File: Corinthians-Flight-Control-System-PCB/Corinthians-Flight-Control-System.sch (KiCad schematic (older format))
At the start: 81 parts, among them J0 RaspberryPi, J1 50ohm Coaxial Ant, J10 M8, J11 M9, J12 M10, J2 GPS/Compass, J3 M1, J4 M2, J5 M3, J6 M4, J7 M5, J8 M6, J9 M7, SW1 BootSW, SW2 SW_DIP_x01, SW3 SW_s, U1 STM32F103C8Tx, U2 LSM6DS3, U3 BMP280, U4 NRF24L01, U5 IST8310, U6 AMS1117-3.3, U7 AMS1117-5.0, Y1 8Mhz, Y2 16Mhz

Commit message: New corrections and CAD files
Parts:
- F1: value 500mA -> 3A
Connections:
- net CE: now also U1.26 (PB13); no longer U1.14 (PA4)
- net CSN: now also U1.27 (PB14); no longer U1.15 (PA5)
- net MISO: now also U1.16 (PA6); no longer U1.40 (PB4)
- net MOSI: now also U1.17 (PA7); no longer U1.41 (PB5)
- net PWM1-E: now also U1.40 (PB4); no longer U1.26 (PB13)
- net PWM1-F: now also U1.41 (PB5); no longer U1.27 (PB14)
- net PWM1-G: now also U1.18 (PB0); no longer U1.28 (PB15)
- net SCK: now also U1.15 (PA5); no longer U1.39 (PB3)
- net SW_s: now also U1.28 (PB15)
- no-connect marks 53 -> 52
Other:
- moved on the sheet: R4, R5
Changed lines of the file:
@@
 Wire Wire Line
 	10100 3200 10100 3150
-Text GLabel 9100 5400 0    50   Input ~ 0
+Text GLabel 8600 5400 0    50   Input ~ 0
 SDA
-Text GLabel 9100 5300 0    50   Input ~ 0
-SCL
 Text GLabel 10600 5400 2    50   Input ~ 0
 PWM1-B
@@
 Text GLabel 10600 5600 2    50   Input ~ 0
 PWM1-D
-Text GLabel 9100 6000 0    50   Input ~ 0
+Text GLabel 9150 4500 0    50   Input ~ 0
 PWM1-G
-Text GLabel 9100 5900 0    50   Input ~ 0
+Text GLabel 9150 5000 0    50   Input ~ 0
 PWM1-F
-Text GLabel 9100 5800 0    50   Input ~ 0
+Text GLabel 9150 4900 0    50   Input ~ 0
 PWM1-E
 Wire Wire Line
@@
 Wire Wire Line
 	8350 4200 8350 4150
-Text GLabel 9100 5000 0    50   Input ~ 0
+Text GLabel 10600 5200 2    50   Input ~ 0
 MOSI
-Text GLabel 9100 4900 0    50   Input ~ 0
-MISO
-Text GLabel 9100 4800 0    50   Input ~ 0
+Text GLabel 10600 5000 2    50   Input ~ 0
 SCK
 $Comp
@@
 	8350 3750 8350 4150
 Wire Wire Line
-	9100 6000 9200 6000
-Wire Wire Line
-	9100 5900 9200 5900
-Wire Wire Line
-	9100 5800 9200 5800
-Wire Wire Line
 	9100 5700 9200 5700
 Wire Wire Line
@@
 	9100 5500 9200 5500
 Wire Wire Line
-	9100 5400 9150 5400
-Wire Wire Line
 	9100 5200 9200 5200
 Wire Wire Line
 	9100 5100 9200 5100
 Wire Wire Line
-	9100 5000 9200 5000
-Wire Wire Line
-	9100 4900 9200 4900
-Wire Wire Line
-	9100 4800 9200 4800
+	10600 5200 10500 5200
 Wire Wire Line
 	10550 5800 10500 5800
@@
 NoConn ~ 1500 6100
 NoConn ~ 10500 5700
-NoConn ~ 10500 5200
-NoConn ~ 10500 5100
-NoConn ~ 9200 4500
-NoConn ~ 9200 4600
-NoConn ~ 9200 4700
 Wire Wire Line
 	6250 1150 6400 1150
@@
 L Device:R_Small R5
 U 1 1 5FAD2178
-P 8850 5200
-F 0 "R5" V 8654 5200 50  0000 C CNN
-F 1 "4.7K" V 8745 5200 50  0000 C CNN
-F 2 "Resistor_SMD:R_0402_1005Metric" H 8850 5200 50  0001 C CNN
-F 3 "~" H 8850 5200 50  0001 C CNN
-	1    8850 5200
+P 8650 5150
+F 0 "R5" V 8454 5150 50  0000 C CNN
+F 1 "4.7K" V 8545 5150 50  0000 C CNN
+F 2 "Resistor_SMD:R_0402_1005Metric" H 8650 5150 50  0001 C CNN
+F 3 "~" H 8650 5150 50  0001 C CNN
+	1    8650 5150
 	1    0    0    -1
 $EndComp
@@
 L power:+3.3V #PWR0131
 U 1 1 5FB2B0E2
-P 8850 4700
-F 0 "#PWR0131" H 8850 4550 50  0001 C CNN
-F 1 "+3.3V" H 8865 4873 50  0000 C CNN
-F 2 "" H 8850 4700 50  0001 C CNN
-F 3 "" H 8850 4700 50  0001 C CNN
-	1    8850 4700
+P 8650 4700
+F 0 "#PWR0131" H 8650 4550 50  0001 C CNN
+F 1 "+3.3V" H 8665 4873 50  0000 C CNN
+F 2 "" H 8650 4700 50  0001 C CNN
+F 3 "" H 8650 4700 50  0001 C CNN
+	1    8650 4700
 	1    0    0    -1
 $EndComp
@@
 L power:+3.3V #PWR0152
 U 1 1 5FB3CB59
-P 8600 5050
-F 0 "#PWR0152" H 8600 4900 50  0001 C CNN
-F 1 "+3.3V" H 8615 5223 50  0000 C CNN
-F 2 "" H 8600 5050 50  0001 C CNN
-F 3 "" H 8600 5050 50  0001 C CNN
-	1    8600 5050
-	1    0    0    -1
-$EndComp
-Wire Wire Line
-	8850 5100 8850 4700
-Wire Wire Line
-	9100 5300 9150 5300
-Wire Wire Line
-	8900 5350 9150 5350
-Wire Wire Line
-	9150 5350 9150 5400
-Connection ~ 9150 5400
-Wire Wire Line
-	9150 5400 9200 5400
-Wire Wire Line
-	8850 5300 8900 5300
-Wire Wire Line
-	8900 5300 8900 5250
-Wire Wire Line
-	8900 5250 9150 5250
-Wire Wire Line
-	9150 5250 9150 5300
-Connection ~ 9150 5300
-Wire Wire Line
-	9150 5300 9200 5300
-Wire Wire Line
-	8600 5350 8600 5050
+P 8350 4700
+F 0 "#PWR0152" H 8350 4550 50  0001 C CNN
+F 1 "+3.3V" H 8365 4873 50  0000 C CNN
+F 2 "" H 8350 4700 50  0001 C CNN
+F 3 "" H 8350 4700 50  0001 C CNN
+	1    8350 4700
+	1    0    0    -1
+$EndComp
 $Comp
 L Device:R_Small R4
 U 1 1 5FABF7FE
-P 8600 5450
-F 0 "R4" V 8404 5450 50  0000 C CNN
-F 1 "4.7K" V 8495 5450 50  0000 C CNN
-F 2 "Resistor_SMD:R_0402_1005Metric" H 8600 5450 50  0001 C CNN
-F 3 "~" H 8600 5450 50  0001 C CNN
-	1    8600 5450
+P 8350 5150
+F 0 "R4" V 8154 5150 50  0000 C CNN
+F 1 "4.7K" V 8245 5150 50  0000 C CNN
+F 2 "Resistor_SMD:R_0402_1005Metric" H 8350 5150 50  0001 C CNN
+F 3 "~" H 8350 5150 50  0001 C CNN
+	1    8350 5150
 	1    0    0    -1
 $EndComp
@@
 	8550 4350 8550 4150
 Connection ~ 8550 4150
-Text GLabel 10600 4900 2    50   Input ~ 0
+Text GLabel 9100 5800 0    50   Input ~ 0
 CE
-Wire Wire Line
-	10600 4900 10500 4900
 $Comp
 L Switch:SW_DIP_x01 SW2
@@
 Wire Wire Line
 	8150 700  8150 850
-Text GLabel 10600 5000 2    50   Input ~ 0
+Text GLabel 9100 5900 0    50   Input ~ 0
 CSN
-Wire Wire Line
-	10000 6200 9900 6200
-Connection ~ 9900 6200
-Wire Wire Line
-	9900 6200 9800 6200
-Connection ~ 9800 6200
-Wire Wire Line
-	9700 6200 9800 6200
-Wire Wire Line
-	9700 6200 9600 6200
-Connection ~ 9700 6200
-Wire Wire Line
-	10000 3200 9900 3200
-Connection ~ 9900 3200
-Wire Wire Line
-	9800 3200 9900 3200
-Wire Wire Line
-	9700 3200 9800 3200
-Connection ~ 9800 3200
-Connection ~ 9700 3200
-$Comp
-L MCU_ST_STM32F1:STM32F103C8Tx U1
-U 1 1 5F8FC5F0
-P 9900 4700
-F 0 "U1" H 9850 3111 50  0000 C CNN
-F 1 "STM32F103C8Tx" H 9850 3020 39  0000 C CNN
-F 2 "Package_QFP:LQFP-48_7x7mm_P0.5mm" H 9300 3300 50  0001 R CNN
-F 3 "http://www.st.com/st-web-ui/static/active/en/resource/technical/document/datasheet/CD00161566.pdf" H 9900 4700 50  0001 C CNN
-	1    9900 4700
-	1    0    0    -1
-$EndComp
 Wire Wire Line
 	10600 5000 10500 5000
@@
 P 3000 1000
 F 0 "F1" H 3000 1169 50  0000 C CNN
-F 1 "500mA" H 3000 1086 39  0000 C CNN
+F 1 "3A" H 3000 1086 39  0000 C CNN
 F 2 "Fuse:Fuse_0805_2012Metric" H 3000 1000 50  0001 C CNN
 F 3 "~" H 3000 1000 50  0001 C CNN
@@
 Wire Wire Line
 	2650 800  2650 1000
-Wire Wire Line
-	8600 5550 8900 5550
-Wire Wire Line
-	8900 5550 8900 5350
 Text GLabel 9100 5500 0    50   Input ~ 0
 TX2
@@
 	1    0    0    -1
 $EndComp
+Text GLabel 10600 5100 2    50   Input ~ 0
+MISO
+Connection ~ 9700 3200
+Connection ~ 9800 3200
+Wire Wire Line
+	9700 3200 9800 3200
+Connection ~ 9900 3200
+Wire Wire Line
+	9800 3200 9900 3200
+Wire Wire Line
+	10000 3200 9900 3200
+Connection ~ 9700 6200
+Wire Wire Line
+	9700 6200 9600 6200
+Wire Wire Line
+	9700 6200 9800 6200
+Connection ~ 9800 6200
+Connection ~ 9900 6200
+Wire Wire Line
+	9900 6200 9800 6200
+Wire Wire Line
+	10000 6200 9900 6200
+$Comp
+L MCU_ST_STM32F1:STM32F103C8Tx U1
+U 1 1 5F8FC5F0
+P 9900 4700
+F 0 "U1" H 9850 3111 50  0000 C CNN
+F 1 "STM32F103C8Tx" H 9850 3020 39  0000 C CNN
+F 2 "Package_QFP:LQFP-48_7x7mm_P0.5mm" H 9300 3300 50  0001 R CNN
+F 3 "http://www.st.com/st-web-ui/static/active/en/resource/technical/document/datasheet/CD00161566.pdf" H 9900 4700 50  0001 C CNN
+	1    9900 4700
+	1    0    0    -1
+$EndComp
+Wire Wire Line
+	10500 5100 10600 5100
+Wire Wire Line
+	8650 5050 8650 4700
+Wire Wire Line
+	8650 5250 8650 5300
+Connection ~ 8650 5300
+Wire Wire Line
+	8650 5300 8600 5300
+Text GLabel 8600 5300 0    50   Input ~ 0
+SCL
+Wire Wire Line
+	8650 5400 8650 5350
+Wire Wire Line
+	8650 5350 8350 5350
+Wire Wire Line
+	8350 5350 8350 5250
+Connection ~ 8650 5400
+Wire Wire Line
+	8650 5400 8600 5400
+Wire Wire Line
+	8350 5050 8350 4700
+Wire Wire Line
+	9150 4900 9200 4900
+Wire Wire Line
+	9150 5000 9200 5000
+Wire Wire Line
+	9150 4500 9200 4500
+Wire Wire Line
+	8650 5300 9200 5300
+Wire Wire Line
+	8650 5400 9200 5400
+Text GLabel 9100 6000 0    50   Input ~ 0
+SW_s
+NoConn ~ 9200 4700
+NoConn ~ 9200 4800
+Wire Wire Line
+	9100 5800 9200 5800
+Wire Wire Line
+	9100 5900 9200 5900
+NoConn ~ 10500 4900
+Wire Wire Line
+	9100 6000 9200 6000
+NoConn ~ 9200 4600
 $EndSCHEMATC

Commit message: updates
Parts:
- removed R15: 10K, Resistor_SMD:R_0402_1005Metric, symbol Device:R_Small
- added C30: 0.1uF, Capacitor_SMD:C_0402_1005Metric, symbol Device:C_Small
- C10, C11, C19, C20: footprint Capacitor_SMD:C_0603_1608Metric -> Capacitor_SMD:C_0805_2012Metric
- renumbered R14 to R10, R16 to R11, R17 to R12
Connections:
- net GND: now also SW2.1, C30.1, C30.2
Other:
- note added: "3.3v linear voltage regulator\npowers all ICs and smd components\nInput from ESC 5v BEC 0805 caps"
- note added: "5v regulator for external\nGPS and Compass. Input\nfrom ESC 5v BEC, 0805 C, 0805 F1, D6, FB1"
- note removed: "3.3v linear voltage regulator\npowers all ICs and smd components\nInput from ESC 5v BEC 0603 caps"
- note removed: "5v regulator for external\nGPS and Compass. Input\nfrom ESC 5v BEC, 0603 C, 0805 F1, D6, FB1"
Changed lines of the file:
@@
 	5900 550  5900 1850
-Wire Notes Line
-	5900 1850 4450 1850
 Wire Notes Line
 	4450 1850 4450 550
@@
 Wire Notes Line
 	5250 2200 5250 4200
-Wire Notes Line
-	3050 2200 5250 2200
 NoConn ~ 3450 3550
 NoConn ~ 3450 2950
@@
 F 0 "C11" H 2192 1338 50  0000 L CNN
 F 1 "10uF" H 2192 1255 39  0000 L CNN
-F 2 "Capacitor_SMD:C_0603_1608Metric" H 2100 1300 50  0001 C CNN
+F 2 "Capacitor_SMD:C_0805_2012Metric" H 2100 1300 50  0001 C CNN
 F 3 "~" H 2100 1300 50  0001 C CNN
 	1    2100 1300
@@
 F 0 "C10" H 1542 1338 50  0000 L CNN
 F 1 "10uF" H 1542 1255 39  0000 L CNN
-F 2 "Capacitor_SMD:C_0603_1608Metric" H 1450 1300 50  0001 C CNN
+F 2 "Capacitor_SMD:C_0805_2012Metric" H 1450 1300 50  0001 C CNN
 F 3 "~" H 1450 1300 50  0001 C CNN
 	1    1450 1300
@@
 Connection ~ 8350 4150
 $Comp
-L Device:R_Small R14
+L Device:R_Small R10
 U 1 1 5FC8FB39
 P 8650 4350
-F 0 "R14" V 8454 4350 50  0000 C CNN
+F 0 "R10" V 8454 4350 50  0000 C CNN
 F 1 "...." V 8545 4350 50  0000 C CNN
 F 2 "Resistor_SMD:R_0402_1005Metric" H 8650 4350 50  0001 C CNN
@@
 	1    0    0    -1
 $EndComp
-$Comp
-L Device:R_Small R15
-U 1 1 601F7C14
-P 4600 900
-F 0 "R15" V 4796 900 50  0000 C CNN
-F 1 "10K" V 4705 900 39  0000 C CNN
-F 2 "Resistor_SMD:R_0402_1005Metric" H 4600 900 50  0001 C CNN
-F 3 "~" H 4600 900 50  0001 C CNN
-	1    4600 900
-	1    0    0    -1
-$EndComp
 Text GLabel 5550 1300 2    50   Input ~ 0
 NRST
@@
 L power:GND #PWR0153
 U 1 1 6025A3C2
-P 4650 700
-F 0 "#PWR0153" H 4650 450 50  0001 C CNN
-F 1 "GND" H 4655 527 50  0000 C CNN
-F 2 "" H 4650 700 50  0001 C CNN
-F 3 "" H 4650 700 50  0001 C CNN
-	1    4650 700
-	0    -1   -1   0
+P 4600 800
+F 0 "#PWR0153" H 4600 550 50  0001 C CNN
+F 1 "GND" H 4605 627 50  0000 C CNN
+F 2 "" H 4600 800 50  0001 C CNN
+F 3 "" H 4600 800 50  0001 C CNN
+	1    4600 800
+	-1   0    0    1
 $EndComp
 Wire Wire Line
@@
 $EndComp
 $Comp
-L Device:R_Small R16
+L Device:R_Small R11
 U 1 1 60310E55
 P 8150 950
-F 0 "R16" V 7954 950 50  0000 C CNN
+F 0 "R11" V 7954 950 50  0000 C CNN
 F 1 "470" V 8045 950 50  0000 C CNN
 F 2 "Resistor_SMD:R_0402_1005Metric" H 8150 950 50  0001 C CNN
@@
 	5550 1300 5450 1300
 Wire Wire Line
-	4650 700  4600 700
-Wire Wire Line
-	4600 700  4600 800
-Wire Wire Line
 	4950 950  4950 900
 Wire Wire Line
-	4850 1000 4600 1000
-Wire Wire Line
-	4850 1300 4850 1000
+	4850 1050 4600 1050
+Wire Wire Line
+	4850 1300 4850 1050
 Wire Wire Line
 	5700 950  5700 1050
@@
 L power:GND #PWR0177
 U 1 1 605B4224
-P 4650 1250
-F 0 "#PWR0177" H 4650 1000 50  0001 C CNN
-F 1 "GND" H 4655 1077 50  0000 C CNN
-F 2 "" H 4650 1250 50  0001 C CNN
-F 3 "" H 4650 1250 50  0001 C CNN
-	1    4650 1250
+P 4650 1300
+F 0 "#PWR0177" H 4650 1050 50  0001 C CNN
+F 1 "GND" H 4655 1127 50  0000 C CNN
+F 2 "" H 4650 1300 50  0001 C CNN
+F 3 "" H 4650 1300 50  0001 C CNN
+	1    4650 1300
 	-1   0    0    1
 $EndComp
@@
 $EndComp
 $Comp
-L Device:R_Small R17
+L Device:R_Small R12
 U 1 1 605B4230
 P 5200 1450
-F 0 "R17" V 5396 1450 50  0000 C CNN
+F 0 "R12" V 5396 1450 50  0000 C CNN
 F 1 "10K" V 5305 1450 39  0000 C CNN
 F 2 "Resistor_SMD:R_0402_1005Metric" H 5200 1450 50  0001 C CNN
@@
 	4650 1550 4650 1600
 Wire Wire Line
-	4650 1350 4650 1250
+	4650 1350 4650 1300
 Wire Wire Line
 	5400 1450 5400 1650
@@
 All passive smd components are \n0402  unless otherwise stated
 Text Notes 600  1850 0    50   ~ 0
-3.3v linear voltage regulator\npowers all ICs and smd components\nInput from ESC 5v BEC 0603 caps
+3.3v linear voltage regulator\npowers all ICs and smd components\nInput from ESC 5v BEC 0805 caps
 Text Notes 600  4200 0    50   ~ 0
 Internal compass IC
@@
 $EndComp
 Text Notes 2550 1850 0    50   ~ 0
-5v regulator for external\nGPS and Compass. Input\nfrom ESC 5v BEC, 0603 C, 0805 F1, D6, FB1
+5v regulator for external\nGPS and Compass. Input\nfrom ESC 5v BEC, 0805 C, 0805 F1, D6, FB1
 $Comp
 L power:+5VD #PWR0138
@@
 F 0 "C20" H 4092 1338 50  0000 L CNN
 F 1 "10uF" H 4092 1255 39  0000 L CNN
-F 2 "Capacitor_SMD:C_0603_1608Metric" H 4000 1300 50  0001 C CNN
+F 2 "Capacitor_SMD:C_0805_2012Metric" H 4000 1300 50  0001 C CNN
 F 3 "~" H 4000 1300 50  0001 C CNN
 	1    4000 1300
@@
 F 0 "C19" H 3442 1338 50  0000 L CNN
 F 1 "10uF" H 3442 1255 39  0000 L CNN
-F 2 "Capacitor_SMD:C_0603_1608Metric" H 3350 1300 50  0001 C CNN
+F 2 "Capacitor_SMD:C_0805_2012Metric" H 3350 1300 50  0001 C CNN
 F 3 "~" H 3350 1300 50  0001 C CNN
 	1    3350 1300
@@
 	9100 6000 9200 6000
 NoConn ~ 9200 4600
+$Comp
+L Device:C_Small C30
+U 1 1 610C7966
+P 4750 950
+F 0 "C30" H 4842 988 50  0000 L CNN
+F 1 "0.1uF" H 4842 905 39  0000 L CNN
+F 2 "Capacitor_SMD:C_0402_1005Metric" H 4750 950 50  0001 C CNN
+F 3 "~" H 4750 950 50  0001 C CNN
+	1    4750 950
+	0    -1   -1   0
+$EndComp
+Wire Notes Line
+	3050 2200 5250 2200
+Wire Notes Line
+	5900 1850 4450 1850
+Wire Wire Line
+	4600 1050 4600 950
+Wire Wire Line
+	4600 950  4650 950
+Connection ~ 4600 950
+Wire Wire Line
+	4600 850  4850 850
+Wire Wire Line
+	4850 850  4850 950
+Connection ~ 4600 850
+Wire Wire Line
+	4600 850  4600 950
+Wire Wire Line
+	4600 800  4600 850
 $EndSCHEMATC

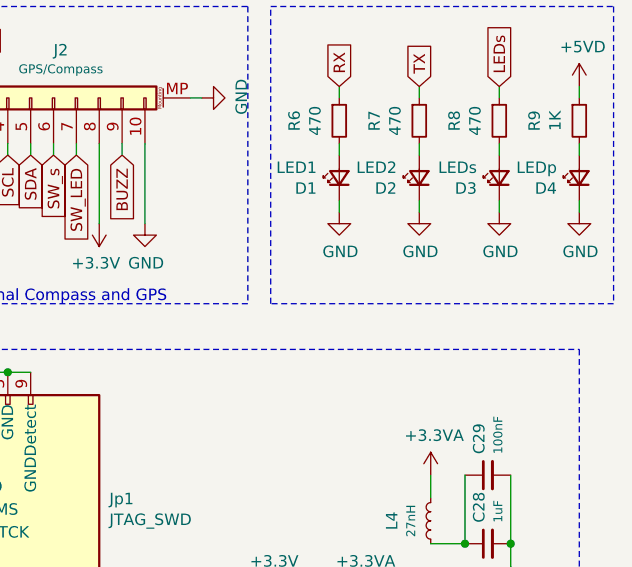
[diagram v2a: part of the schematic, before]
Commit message: schematic and pcb routing update
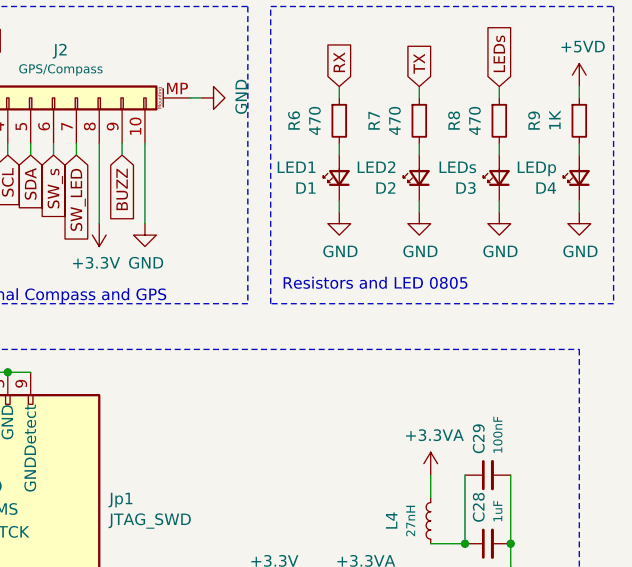
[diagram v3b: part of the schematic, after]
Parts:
- D1, D2, D3, D4: footprint LED_SMD:LED_0402_1005Metric -> LED_SMD:LED_0805_2012Metric
- R6, R7, R8, R9: footprint Resistor_SMD:R_0402_1005Metric -> Resistor_SMD:R_0805_2012Metric
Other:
- note added: "Resistors and LED 0805"
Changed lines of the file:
@@
 F 0 "D4" V 11004 1398 50  0000 L CNN
 F 1 "LEDp" V 11095 1398 50  0000 L CNN
-F 2 "LED_SMD:LED_0402_1005Metric" V 11050 1300 50  0001 C CNN
+F 2 "LED_SMD:LED_0805_2012Metric" V 11050 1300 50  0001 C CNN
 F 3 "~" V 11050 1300 50  0001 C CNN
 	1    11050 1300
@@
 F 0 "D2" V 10304 1398 50  0000 L CNN
 F 1 "LED2" V 10395 1398 50  0000 L CNN
-F 2 "LED_SMD:LED_0402_1005Metric" V 10350 1300 50  0001 C CNN
+F 2 "LED_SMD:LED_0805_2012Metric" V 10350 1300 50  0001 C CNN
 F 3 "~" V 10350 1300 50  0001 C CNN
 	1    10350 1300
@@
 F 0 "D1" V 9954 1398 50  0000 L CNN
 F 1 "LED1" V 10045 1398 50  0000 L CNN
-F 2 "LED_SMD:LED_0402_1005Metric" V 10000 1300 50  0001 C CNN
+F 2 "LED_SMD:LED_0805_2012Metric" V 10000 1300 50  0001 C CNN
 F 3 "~" V 10000 1300 50  0001 C CNN
 	1    10000 1300
@@
 F 0 "R9" V 10854 1050 50  0000 C CNN
 F 1 "1K" V 10945 1050 50  0000 C CNN
-F 2 "Resistor_SMD:R_0402_1005Metric" H 11050 1050 50  0001 C CNN
+F 2 "Resistor_SMD:R_0805_2012Metric" H 11050 1050 50  0001 C CNN
 F 3 "~" H 11050 1050 50  0001 C CNN
 	1    11050 1050
@@
 F 0 "R8" V 10504 1050 50  0000 C CNN
 F 1 "470" V 10595 1050 50  0000 C CNN
-F 2 "Resistor_SMD:R_0402_1005Metric" H 10700 1050 50  0001 C CNN
+F 2 "Resistor_SMD:R_0805_2012Metric" H 10700 1050 50  0001 C CNN
 F 3 "~" H 10700 1050 50  0001 C CNN
 	1    10700 1050
@@
 F 0 "R7" V 10154 1050 50  0000 C CNN
 F 1 "470" V 10245 1050 50  0000 C CNN
-F 2 "Resistor_SMD:R_0402_1005Metric" H 10350 1050 50  0001 C CNN
+F 2 "Resistor_SMD:R_0805_2012Metric" H 10350 1050 50  0001 C CNN
 F 3 "~" H 10350 1050 50  0001 C CNN
 	1    10350 1050
@@
 F 0 "R6" V 9804 1050 50  0000 C CNN
 F 1 "470" V 9895 1050 50  0000 C CNN
-F 2 "Resistor_SMD:R_0402_1005Metric" H 10000 1050 50  0001 C CNN
+F 2 "Resistor_SMD:R_0805_2012Metric" H 10000 1050 50  0001 C CNN
 F 3 "~" H 10000 1050 50  0001 C CNN
 	1    10000 1050
@@
 F 0 "D3" V 10654 1398 50  0000 L CNN
 F 1 "LEDs" V 10745 1398 50  0000 L CNN
-F 2 "LED_SMD:LED_0402_1005Metric" V 10700 1300 50  0001 C CNN
+F 2 "LED_SMD:LED_0805_2012Metric" V 10700 1300 50  0001 C CNN
 F 3 "~" V 10700 1300 50  0001 C CNN
 	1    10700 1300
@@
 Wire Wire Line
 	4600 800  4600 850
+Text Notes 9750 1800 0    50   ~ 0
+Resistors and LED 0805
 $EndSCHEMATC

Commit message: Routing finished ?
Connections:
- net +3V3 is gone; now on net +3.3VA: C11.1, C12.2, C13.1, C14.1, C15.1, C16.2, C17.2, C21.2, C22.2, C23.2, C24.2, C25.2, C8.2, C9.2, J2.8 (Pin_8), Jp1.1 (VTref), R4.1, R5.1, SW1.1 (A), SW3.1 (A), U1.1 (VBAT), U1.24 (VDD), U1.36 (VDD), U1.48 (VDD), U2.5 (VDDIO), U2.8 (VDD), U3.2 (CSB), U3.6 (VDDIO), U3.8 (VDD), U4.15 (VDD), U4.18 (VDD), U4.7 (VDD), U5.13 (DVDD), U5.2 (AVDD), U6.2 (VO)
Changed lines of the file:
@@
 Text Notes 9750 1800 0    50   ~ 0
 Resistors and LED 0805
+Wire Wire Line
+	10000 3200 10100 3200
+Connection ~ 10000 3200
+Connection ~ 10100 3200
 $EndSCHEMATC

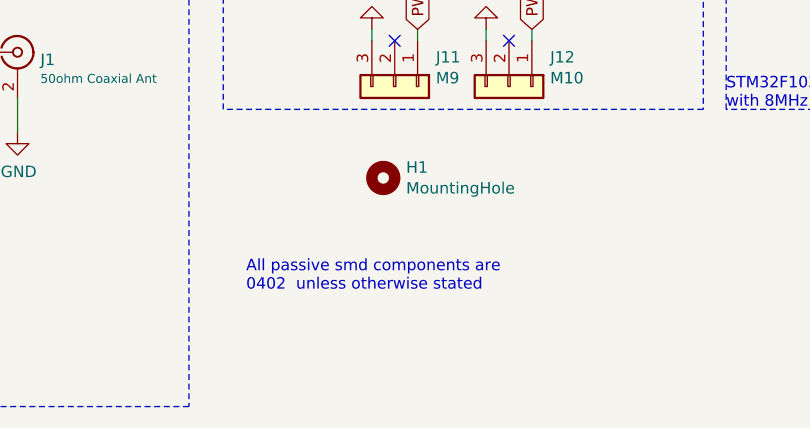
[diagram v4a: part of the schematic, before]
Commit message: 0402 components changed to 0805
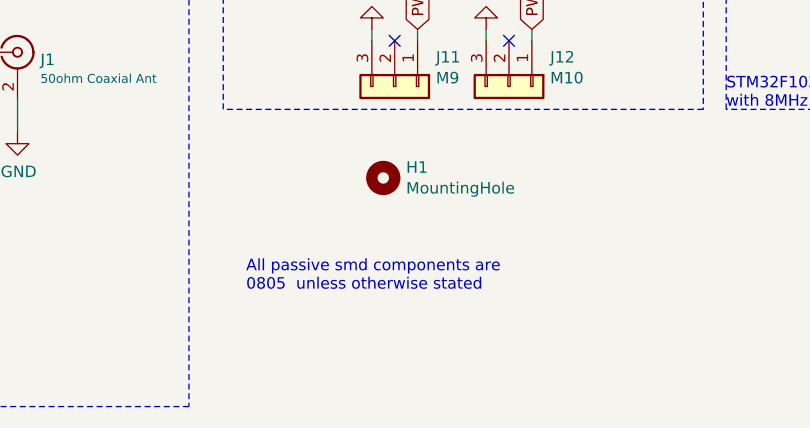
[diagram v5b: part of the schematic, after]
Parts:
- C1, C12, C13, C14, C15, C16, C17, C18, C2, C21, C22, C23, C24, C25, C26, C27, C28, C29, C3, C30, C4, C5, C6, C7, C8, C9: footprint Capacitor_SMD:C_0402_1005Metric -> Capacitor_SMD:C_0805_2012Metric_Pad1.15x1.40mm_HandSolder
- C10, C11, C19, C20: footprint Capacitor_SMD:C_0805_2012Metric -> Capacitor_SMD:C_0805_2012Metric_Pad1.15x1.40mm_HandSolder
- D1, D2, D3, D4: footprint LED_SMD:LED_0805_2012Metric -> LED_SMD:LED_0805_2012Metric_Pad1.15x1.40mm_HandSolder
- D5: footprint LED_SMD:LED_0402_1005Metric -> LED_SMD:LED_0805_2012Metric_Pad1.15x1.40mm_HandSolder
- D6: footprint Diode_SMD:D_0805_2012Metric -> Diode_SMD:D_0805_2012Metric_Pad1.15x1.40mm_HandSolder
- F1: footprint Fuse:Fuse_0805_2012Metric -> Fuse:Fuse_0805_2012Metric_Pad1.15x1.40mm_HandSolder
- FB1: footprint Inductor_SMD:L_0805_2012Metric -> Inductor_SMD:L_0805_2012Metric_Pad1.15x1.40mm_HandSolder
- L1, L2, L3, L4: footprint Inductor_SMD:L_0402_1005Metric -> Inductor_SMD:L_0805_2012Metric_Pad1.15x1.40mm_HandSolder
- R1, R10, R11, R12, R2, R3, R4, R5: footprint Resistor_SMD:R_0402_1005Metric -> Resistor_SMD:R_0805_2012Metric_Pad1.15x1.40mm_HandSolder
- R6, R7, R8, R9: footprint Resistor_SMD:R_0805_2012Metric -> Resistor_SMD:R_0805_2012Metric_Pad1.15x1.40mm_HandSolder
- Y1, Y2: footprint Crystal:Crystal_SMD_0603-2Pin_6.0x3.5mm -> Crystal:Crystal_SMD_Abracon_ABM8G-4Pin_3.2x2.5mm
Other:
- note added: "All passive smd components are \n0805 unless otherwise stated"
- note removed: "All passive smd components are \n0402 unless otherwise stated"
